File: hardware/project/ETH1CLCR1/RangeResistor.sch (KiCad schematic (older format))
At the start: 94 parts, among them K1201 TQ2SA-5V, Q1201 2N2218A, Q1202 BC847W, Q1203 2N2904A, Q1204 BC847W, U1201 AQY212GS, U1202 AQY212GS, U1203 AD5293BRUZ-20, U1204 TL072, U1205 AQY212GS, U1206 AQY212GS, U1207 AQY212GS, U1208 AQY212GS, U1209 AQY212GS, U1210 AQY212GS, U1211 AQY212GS, U1212 AQY212GS, U1213 HA3-2525-5Z, U1214 AQY212GS, U1215 AQY212GS

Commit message: PCB layout
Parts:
- added C1218: C, Capacitor_SMD:C_0603_1608Metric_Pad1.05x0.95mm_HandSolder, symbol Device:C
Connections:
- net at C1203.1, R1203.2, R1206.1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: now also C1218.1
- net at C1203.2, R1206.2, R1209.1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: now also C1218.2
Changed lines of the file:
@@
 NoConn ~ 6900 7650
-$Comp
-L ETH1CLCR1:HA3-2525-5Z U1213
-U 1 1 5E257A58
-P 6900 8050
-F 0 "U1213" H 7250 8300 50  0000 L CNN
-F 1 "HA3-2525-5Z" H 7100 8200 50  0000 L CNN
-F 2 "Package_DIP:DIP-8_W7.62mm" H 7550 8700 50  0001 C CNN
-F 3 "" H 7550 8700 50  0001 C CNN
-	1    6900 8050
-	1    0    0    -1
-$EndComp
 $Comp
 L Device:R R1232
@@
 $EndComp
 $Comp
-L ETH1CLCR1:+12VF #PWR01225
-U 1 1 5E591A50
-P 9200 6700
-F 0 "#PWR01225" H 9200 6550 50  0001 C CNN
-F 1 "+12VF" H 9215 6873 50  0000 C CNN
-F 2 "" H 9200 6700 50  0001 C CNN
-F 3 "" H 9200 6700 50  0001 C CNN
-	1    9200 6700
-	1    0    0    -1
-$EndComp
-$Comp
-L ETH1CLCR1:+12VF #PWR01239
-U 1 1 5E591F4C
-P 2400 10200
-F 0 "#PWR01239" H 2400 10050 50  0001 C CNN
-F 1 "+12VF" H 2415 10373 50  0000 C CNN
-F 2 "" H 2400 10200 50  0001 C CNN
-F 3 "" H 2400 10200 50  0001 C CNN
-	1    2400 10200
-	1    0    0    -1
-$EndComp
-$Comp
-L ETH1CLCR1:-12VF #PWR01241
-U 1 1 5E594F18
-P 2400 10800
-F 0 "#PWR01241" H 2400 10650 50  0001 C CNN
-F 1 "-12VF" H 2415 10973 50  0000 C CNN
-F 2 "" H 2400 10800 50  0001 C CNN
-F 3 "" H 2400 10800 50  0001 C CNN
-	1    2400 10800
-	-1   0    0    1
-$EndComp
-$Comp
-L ETH1CLCR1:-12VF #PWR01236
-U 1 1 5E59565C
-P 9200 9400
-F 0 "#PWR01236" H 9200 9250 50  0001 C CNN
-F 1 "-12VF" H 9215 9573 50  0000 C CNN
-F 2 "" H 9200 9400 50  0001 C CNN
-F 3 "" H 9200 9400 50  0001 C CNN
-	1    9200 9400
-	-1   0    0    1
-$EndComp
-$Comp
-L ETH1CLCR1:-12VF #PWR01234
-U 1 1 5E596993
-P 6800 8800
-F 0 "#PWR01234" H 6800 8650 50  0001 C CNN
-F 1 "-12VF" H 6815 8973 50  0000 C CNN
-F 2 "" H 6800 8800 50  0001 C CNN
-F 3 "" H 6800 8800 50  0001 C CNN
-	1    6800 8800
-	-1   0    0    1
-$EndComp
-$Comp
 L Device:R_POT_TRIM RV1202
 U 1 1 5E2BC0E0
@@
 Wire Wire Line
 	5550 7600 5550 7500
-$Comp
-L ETH1CLCR1:+12VF #PWR01229
-U 1 1 5E2CF95E
-P 5750 7300
-F 0 "#PWR01229" H 5750 7150 50  0001 C CNN
-F 1 "+12VF" V 5750 7550 50  0000 C CNN
-F 2 "" H 5750 7300 50  0001 C CNN
-F 3 "" H 5750 7300 50  0001 C CNN
-	1    5750 7300
-	0    1    1    0
-$EndComp
-$Comp
-L ETH1CLCR1:-12VF #PWR01228
-U 1 1 5E2D14F1
-P 5350 7300
-F 0 "#PWR01228" H 5350 7150 50  0001 C CNN
-F 1 "-12VF" V 5350 7550 50  0000 C CNN
-F 2 "" H 5350 7300 50  0001 C CNN
-F 3 "" H 5350 7300 50  0001 C CNN
-	1    5350 7300
-	0    -1   -1   0
-$EndComp
 Wire Wire Line
 	5350 7300 5400 7300
@@
 Wire Wire Line
 	6800 7300 6800 7350
-$Comp
-L ETH1CLCR1:+12VF #PWR01230
-U 1 1 5E5913F4
-P 6800 7300
-F 0 "#PWR01230" H 6800 7150 50  0001 C CNN
-F 1 "+12VF" H 6815 7473 50  0000 C CNN
-F 2 "" H 6800 7300 50  0001 C CNN
-F 3 "" H 6800 7300 50  0001 C CNN
-	1    6800 7300
-	1    0    0    -1
-$EndComp
 Wire Wire Line
 	10500 6250 10500 8050
@@
 $EndComp
 $Comp
-L ETH1CLCR1:+12VF #PWR01242
-U 1 1 5E29F642
-P 3050 10200
-F 0 "#PWR01242" H 3050 10050 50  0001 C CNN
-F 1 "+12VF" H 3065 10373 50  0000 C CNN
-F 2 "" H 3050 10200 50  0001 C CNN
-F 3 "" H 3050 10200 50  0001 C CNN
-	1    3050 10200
-	1    0    0    -1
-$EndComp
-$Comp
 L Device:C C1214
 U 1 1 5E29F808
@@
 F 3 "~" H 3600 10500 50  0001 C CNN
 	1    3600 10500
-	1    0    0    -1
-$EndComp
-$Comp
-L ETH1CLCR1:-12VF #PWR01243
-U 1 1 5E29FA67
-P 3600 10200
-F 0 "#PWR01243" H 3600 10050 50  0001 C CNN
-F 1 "-12VF" H 3615 10373 50  0000 C CNN
-F 2 "" H 3600 10200 50  0001 C CNN
-F 3 "" H 3600 10200 50  0001 C CNN
-	1    3600 10200
 	1    0    0    -1
 $EndComp
@@
 Wire Wire Line
 	3550 6250 3550 6450
+$Comp
+L ETH1CLCR1:-12VF #PWR01228
+U 1 1 5E2D14F1
+P 5350 7300
+F 0 "#PWR01228" H 5350 7150 50  0001 C CNN
+F 1 "-12VF" V 5350 7550 50  0000 C CNN
+F 2 "" H 5350 7300 50  0001 C CNN
+F 3 "" H 5350 7300 50  0001 C CNN
+	1    5350 7300
+	0    -1   -1   0
+$EndComp
+$Comp
+L ETH1CLCR1:-12VF #PWR01236
+U 1 1 5E59565C
+P 9200 9400
+F 0 "#PWR01236" H 9200 9250 50  0001 C CNN
+F 1 "-12VF" H 9215 9573 50  0000 C CNN
+F 2 "" H 9200 9400 50  0001 C CNN
+F 3 "" H 9200 9400 50  0001 C CNN
+	1    9200 9400
+	-1   0    0    1
+$EndComp
+$Comp
+L ETH1CLCR1:+12VF #PWR01225
+U 1 1 5E591A50
+P 9200 6700
+F 0 "#PWR01225" H 9200 6550 50  0001 C CNN
+F 1 "+12VF" H 9215 6873 50  0000 C CNN
+F 2 "" H 9200 6700 50  0001 C CNN
+F 3 "" H 9200 6700 50  0001 C CNN
+	1    9200 6700
+	1    0    0    -1
+$EndComp
+$Comp
+L ETH1CLCR1:+12VF #PWR01229
+U 1 1 5E2CF95E
+P 5750 7300
+F 0 "#PWR01229" H 5750 7150 50  0001 C CNN
+F 1 "+12VF" V 5750 7550 50  0000 C CNN
+F 2 "" H 5750 7300 50  0001 C CNN
+F 3 "" H 5750 7300 50  0001 C CNN
+	1    5750 7300
+	0    1    1    0
+$EndComp
+$Comp
+L ETH1CLCR1:-12VF #PWR01234
+U 1 1 5E596993
+P 6800 8800
+F 0 "#PWR01234" H 6800 8650 50  0001 C CNN
+F 1 "-12VF" H 6815 8973 50  0000 C CNN
+F 2 "" H 6800 8800 50  0001 C CNN
+F 3 "" H 6800 8800 50  0001 C CNN
+	1    6800 8800
+	-1   0    0    1
+$EndComp
+$Comp
+L ETH1CLCR1:+12VF #PWR01230
+U 1 1 5E5913F4
+P 6800 7300
+F 0 "#PWR01230" H 6800 7150 50  0001 C CNN
+F 1 "+12VF" H 6815 7473 50  0000 C CNN
+F 2 "" H 6800 7300 50  0001 C CNN
+F 3 "" H 6800 7300 50  0001 C CNN
+	1    6800 7300
+	1    0    0    -1
+$EndComp
+$Comp
+L ETH1CLCR1:-12VF #PWR01241
+U 1 1 5E594F18
+P 2400 10800
+F 0 "#PWR01241" H 2400 10650 50  0001 C CNN
+F 1 "-12VF" H 2415 10973 50  0000 C CNN
+F 2 "" H 2400 10800 50  0001 C CNN
+F 3 "" H 2400 10800 50  0001 C CNN
+	1    2400 10800
+	-1   0    0    1
+$EndComp
+$Comp
+L ETH1CLCR1:-12VF #PWR01243
+U 1 1 5E29FA67
+P 3600 10200
+F 0 "#PWR01243" H 3600 10050 50  0001 C CNN
+F 1 "-12VF" H 3615 10373 50  0000 C CNN
+F 2 "" H 3600 10200 50  0001 C CNN
+F 3 "" H 3600 10200 50  0001 C CNN
+	1    3600 10200
+	1    0    0    -1
+$EndComp
+$Comp
+L ETH1CLCR1:+12VF #PWR01242
+U 1 1 5E29F642
+P 3050 10200
+F 0 "#PWR01242" H 3050 10050 50  0001 C CNN
+F 1 "+12VF" H 3065 10373 50  0000 C CNN
+F 2 "" H 3050 10200 50  0001 C CNN
+F 3 "" H 3050 10200 50  0001 C CNN
+	1    3050 10200
+	1    0    0    -1
+$EndComp
+$Comp
+L ETH1CLCR1:+12VF #PWR01239
+U 1 1 5E591F4C
+P 2400 10200
+F 0 "#PWR01239" H 2400 10050 50  0001 C CNN
+F 1 "+12VF" H 2415 10373 50  0000 C CNN
+F 2 "" H 2400 10200 50  0001 C CNN
+F 3 "" H 2400 10200 50  0001 C CNN
+	1    2400 10200
+	1    0    0    -1
+$EndComp
+$Comp
+L ETH1CLCR1:HA3-2525-5Z U1213
+U 1 1 5E257A58
+P 6900 8050
+F 0 "U1213" H 7250 8300 50  0000 L CNN
+F 1 "HA3-2525-5Z" H 7100 8200 50  0000 L CNN
+F 2 "Package_DIP:DIP-8_W7.62mm" H 7550 8700 50  0001 C CNN
+F 3 "" H 7550 8700 50  0001 C CNN
+	1    6900 8050
+	1    0    0    -1
+$EndComp
+$Comp
+L Device:C C1218
+U 1 1 5E58CDD7
+P 7500 1900
+F 0 "C1218" V 7248 1900 50  0000 C CNN
+F 1 "C" V 7339 1900 50  0000 C CNN
+F 2 "Capacitor_SMD:C_0603_1608Metric_Pad1.05x0.95mm_HandSolder" H 7538 1750 50  0001 C CNN
+F 3 "~" H 7500 1900 50  0001 C CNN
+	1    7500 1900
+	0    1    1    0
+$EndComp
+Wire Wire Line
+	7350 1900 7150 1900
+Wire Wire Line
+	7150 1900 7150 2300
+Wire Wire Line
+	7650 1900 7850 1900
+Wire Wire Line
+	7850 1900 7850 2300
 $EndSCHEMATC

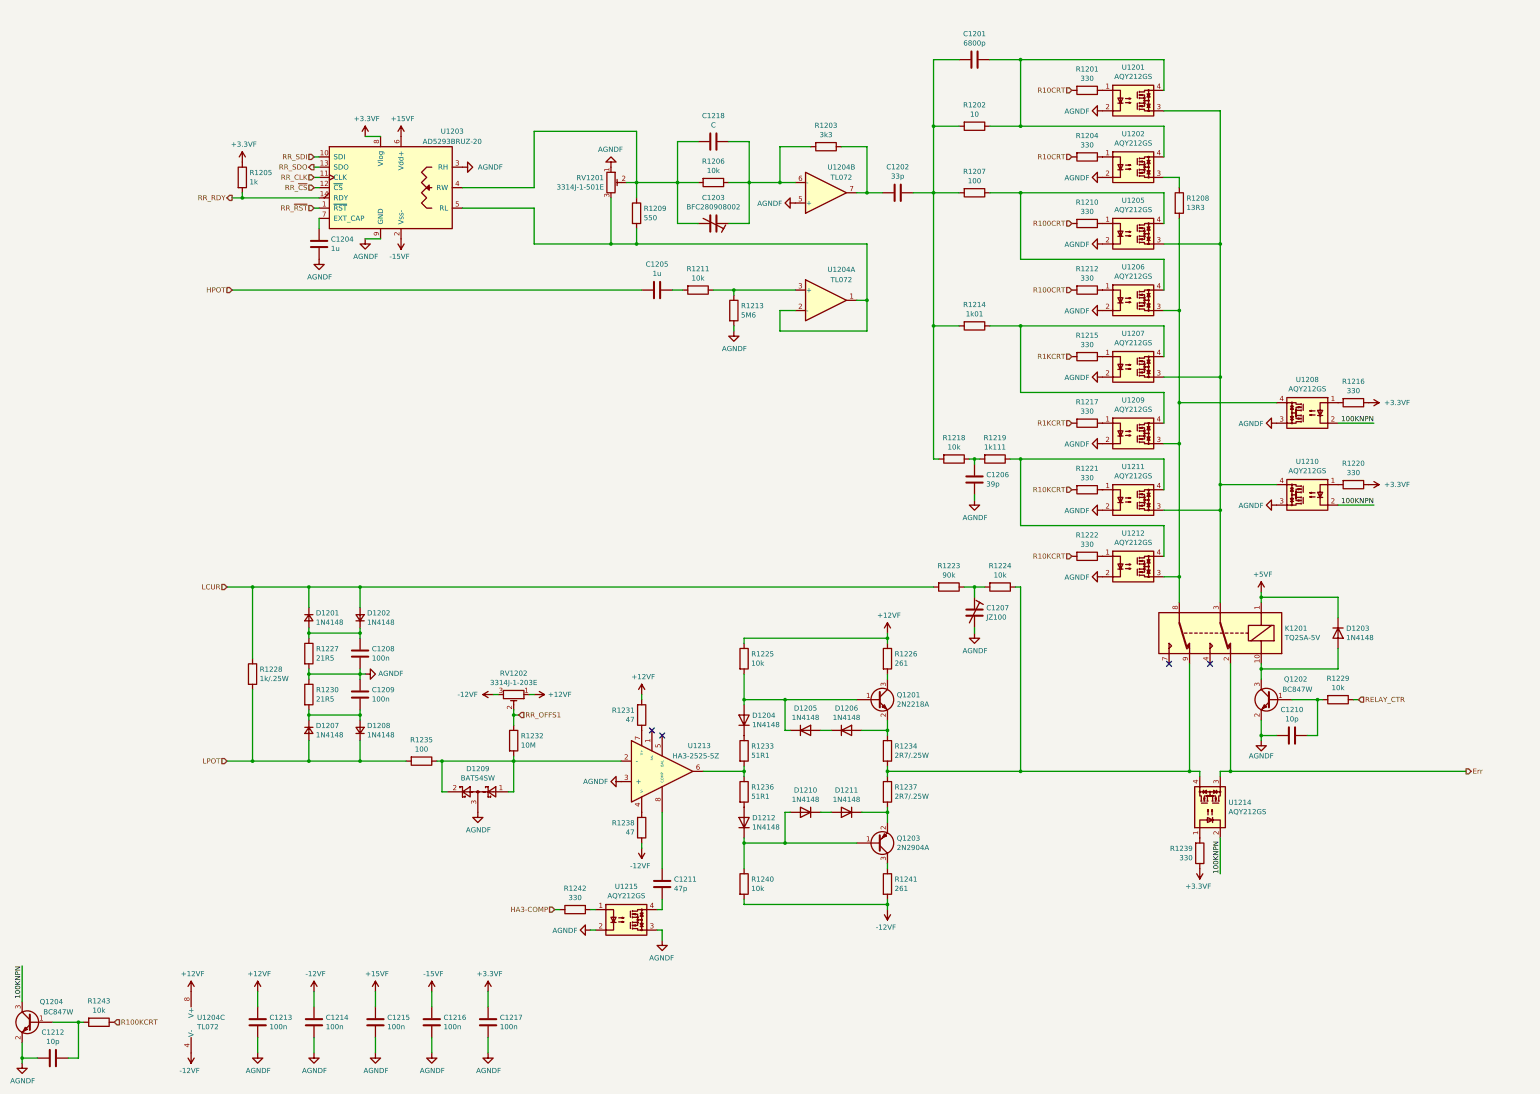
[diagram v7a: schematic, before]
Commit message: Redesinged ADC schematic.
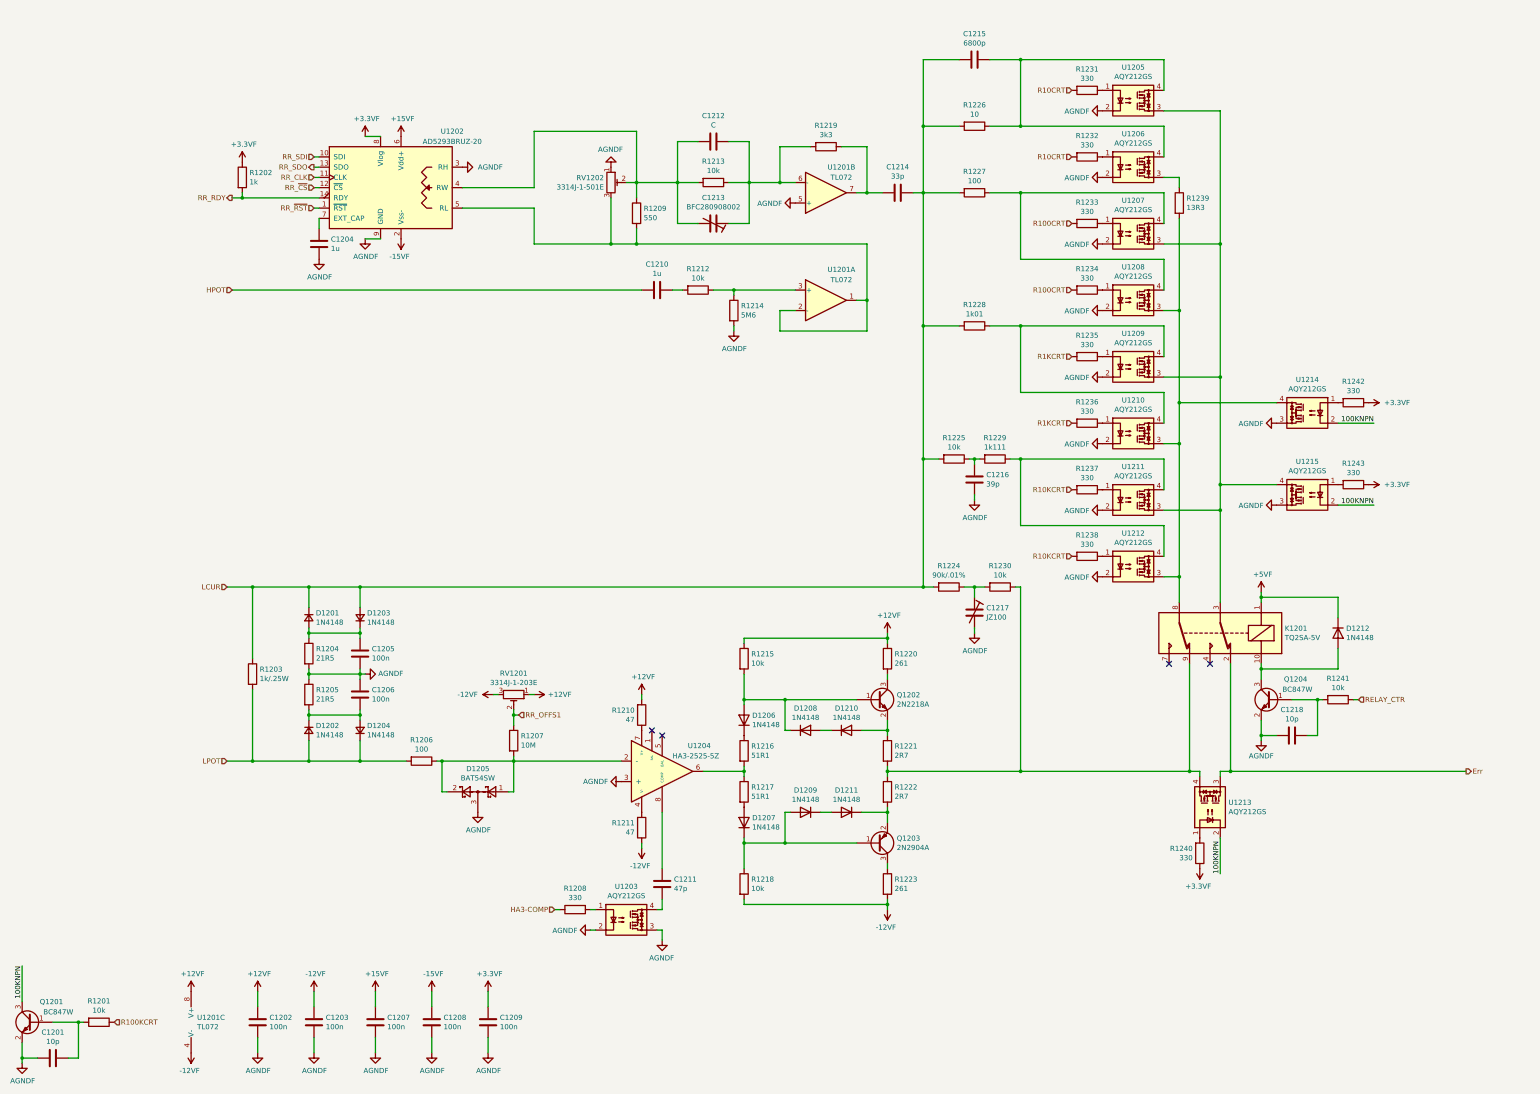
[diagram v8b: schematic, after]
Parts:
- R1221: renamed from R1234; value 2R7/.25W -> 2R7
- R1222: renamed from R1237; value 2R7/.25W -> 2R7
- R1224: renamed from R1223; value 90k -> 90k/.01%
- renumbered C1212 to C1201, C1213 to C1202, C1214 to C1203, C1208 to C1205, C1209 to C1206, C1215 to C1207, C1216 to C1208, C1217 to C1209, C1205 to C1210, C1218 to C1212, C1203 to C1213, C1202 to C1214, C1201 to C1215, C1206 to C1216, C1207 to C1217, C1210 to C1218, D1207 to D1202, D1202 to D1203, D1208 to D1204, D1209 to D1205, D1204 to D1206, D1212 to D1207, D1205 to D1208, D1210 to D1209, D1206 to D1210, D1203 to D1212, Q1204 to Q1201, Q1201 to Q1202, Q1202 to Q1204, R1243 to R1201, R1205 to R1202, R1228 to R1203, R1227 to R1204, R1230 to R1205, R1235 to R1206, R1232 to R1207, R1242 to R1208, R1231 to R1210, R1238 to R1211, R1211 to R1212, R1206 to R1213, R1213 to R1214, R1225 to R1215, R1233 to R1216, R1236 to R1217, R1240 to R1218, R1203 to R1219, R1226 to R1220, R1241 to R1223, R1218 to R1225, R1202 to R1226, R1207 to R1227, R1214 to R1228, R1219 to R1229, R1224 to R1230, R1201 to R1231, R1204 to R1232, R1210 to R1233, R1212 to R1234, R1215 to R1235, R1217 to R1236, R1221 to R1237, R1222 to R1238, R1208 to R1239, R1239 to R1240, R1229 to R1241, R1216 to R1242, R1220 to R1243, RV1202 to RV1201, RV1201 to RV1202, U1204 to U1201, U1203 to U1202, U1215 to U1203, U1213 to U1204, U1201 to U1205, U1202 to U1206, U1205 to U1207, U1206 to U1208, U1207 to U1209, U1209 to U1210, U1214 to U1213, U1208 to U1214, U1210 to U1215
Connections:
- net LCUR: now also C1214.1, C1215.2, R1225.2, R1226.2, R1227.2, R1228.2
